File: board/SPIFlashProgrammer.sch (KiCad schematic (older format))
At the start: 0 parts

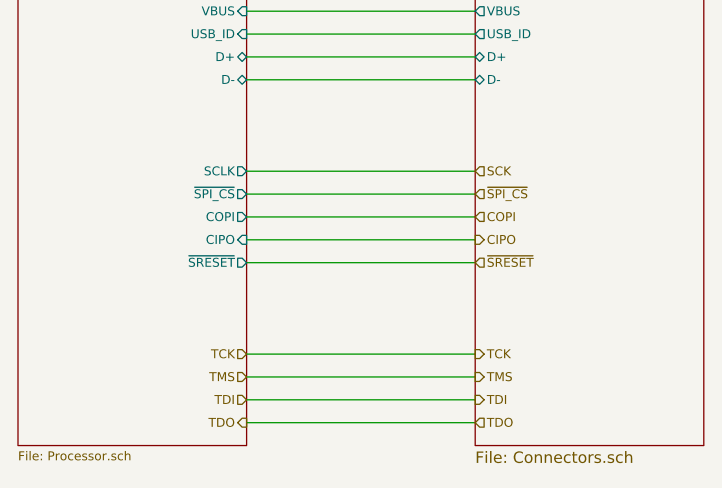
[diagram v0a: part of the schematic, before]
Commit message: Fixed all the top-level wiring that was wrong because the pin types it was connected with were wrong
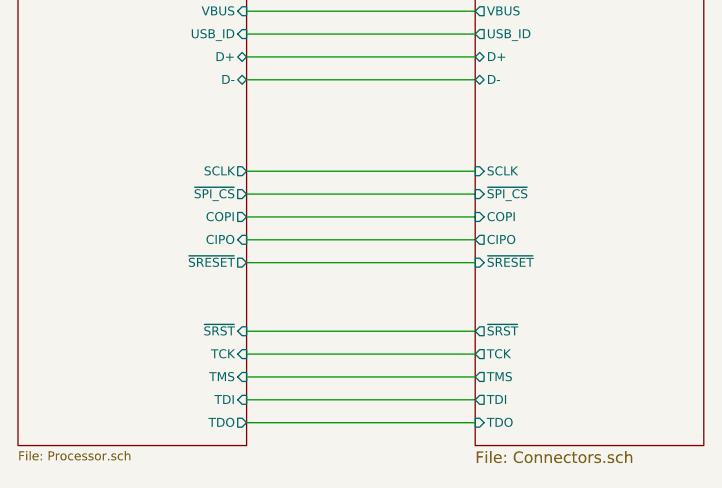
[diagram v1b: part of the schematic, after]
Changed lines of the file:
@@
 Comment4 ""
 $EndDescr
-Text HLabel 5250 5150 0    39   Output ~ 0
-TDO
-Text HLabel 5250 5050 0    39   Input ~ 0
-TDI
-Text HLabel 5250 4950 0    39   Input ~ 0
-TMS
-Text HLabel 5250 4850 0    39   Input ~ 0
-TCK
-Text HLabel 6250 4050 2    39   Input ~ 0
-SCK
-Text HLabel 6250 4150 2    39   Input ~ 0
-~SPI_CS
-Text HLabel 6250 4250 2    39   Input ~ 0
-COPI
-Text HLabel 6250 4350 2    39   Output ~ 0
-CIPO
-Text HLabel 6250 4450 2    39   Input ~ 0
-~SRESET
-Text HLabel 6250 4850 2    39   Output ~ 0
-TCK
-Text HLabel 6250 4950 2    39   Output ~ 0
-TMS
-Text HLabel 6250 5050 2    39   Output ~ 0
-TDI
-Text HLabel 6250 5150 2    39   Input ~ 0
-TDO
 Wire Wire Line
 	5250 3350 6250 3350
@@
 	5250 5150 6250 5150
 $Sheet
+S 6250 3250 1000 2000
+U 5F0A82B6
+F0 "Connectors" 50
+F1 "Connectors.sch" 50
+F2 "D-" B L 6250 3650 39
+F3 "D+" B L 6250 3550 39
+F4 "USB_ID" O L 6250 3450 39
+F5 "VBUS" O L 6250 3350 39
+F6 "CIPO" O L 6250 4350 39
+F7 "SCLK" I L 6250 4050 39
+F8 "~SPI_CS" I L 6250 4150 39
+F9 "~SRESET" I L 6250 4450 39
+F10 "COPI" I L 6250 4250 39
+F11 "TMS" O L 6250 4950 39
+F12 "TCK" O L 6250 4850 39
+F13 "TDO" I L 6250 5150 39
+F14 "TDI" O L 6250 5050 39
+F15 "~SRST" O L 6250 4750 39
+$EndSheet
+$Sheet
 S 4250 3250 1000 2000
 U 5F0A81B1
@@
 F9 "D-" B R 5250 3650 39
 F10 "D+" B R 5250 3550 39
+F11 "TCK" I R 5250 4850 39
+F12 "TMS" I R 5250 4950 39
+F13 "TDI" I R 5250 5050 39
+F14 "TDO" O R 5250 5150 39
+F15 "~SRST" I R 5250 4750 39
 $EndSheet
-$Sheet
-S 6250 3250 1000 2000
-U 5F0A82B6
-F0 "Connectors" 50
-F1 "Connectors.sch" 50
-F2 "D-" B L 6250 3650 39
-F3 "D+" B L 6250 3550 39
-F4 "USB_ID" O L 6250 3450 39
-F5 "VBUS" O L 6250 3350 39
-$EndSheet
+Wire Wire Line
+	5250 4750 6250 4750
 $EndSCHEMATC

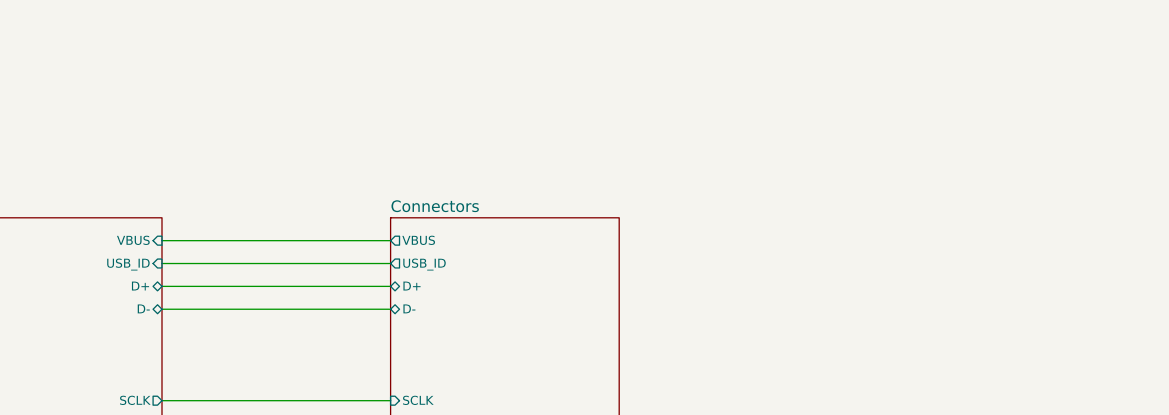
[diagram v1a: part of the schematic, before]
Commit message: Added the work to the schematic from the last stream, and updated all the footprints to reflect the work going in on my symbol and footprint libraries
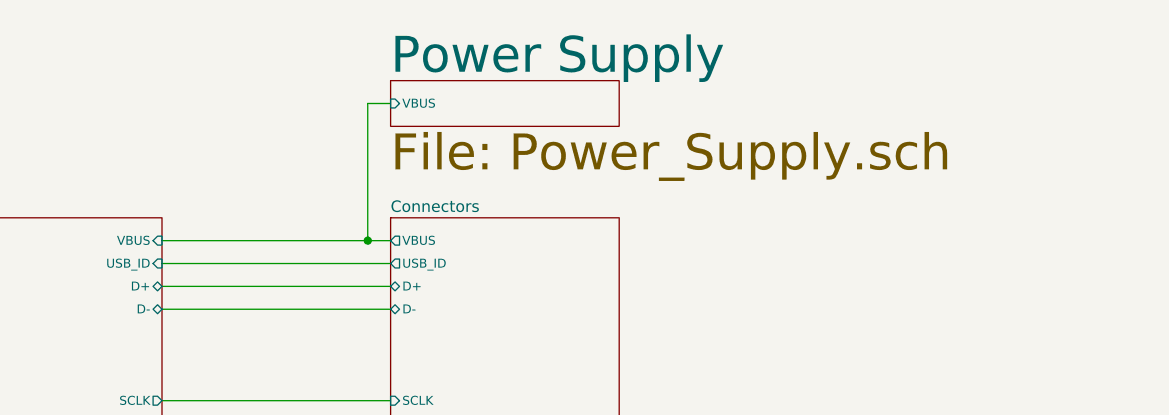
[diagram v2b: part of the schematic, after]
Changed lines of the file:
@@
 $Descr A4 11693 8268
 encoding utf-8
-Sheet 1 3
-Title ""
+Sheet 1 4
+Title "Top-level Schematic"
 Date ""
-Rev ""
-Comp ""
+Rev "R1"
+Comp "Rachel Mant"
 Comment1 ""
 Comment2 ""
@@
 $EndDescr
 Wire Wire Line
-	5250 3350 6250 3350
+	5250 3350 6150 3350
 Wire Wire Line
 	6250 3450 5250 3450
@@
 Wire Wire Line
 	5250 4750 6250 4750
+$Sheet
+S 6250 2650 1000 200
+U 5F6E308F
+F0 "Power Supply" 157
+F1 "Power_Supply.sch" 157
+F2 "VBUS" I L 6250 2750 39
+$EndSheet
+Wire Wire Line
+	6250 2750 6150 2750
+Wire Wire Line
+	6150 2750 6150 3350
+Connection ~ 6150 3350
+Wire Wire Line
+	6150 3350 6250 3350
 $EndSCHEMATC

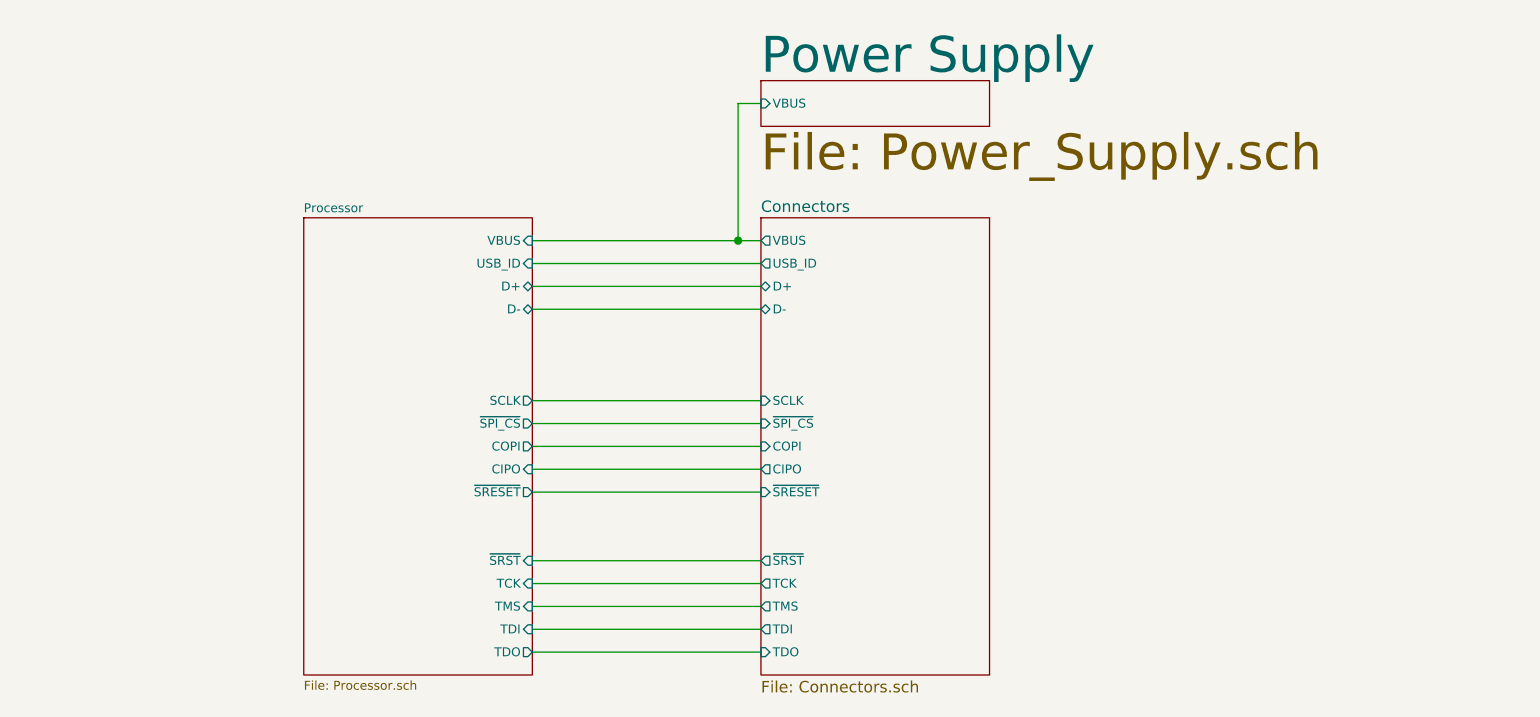
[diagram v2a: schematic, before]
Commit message: Added the two Flash devices and the user buttons to the schematic
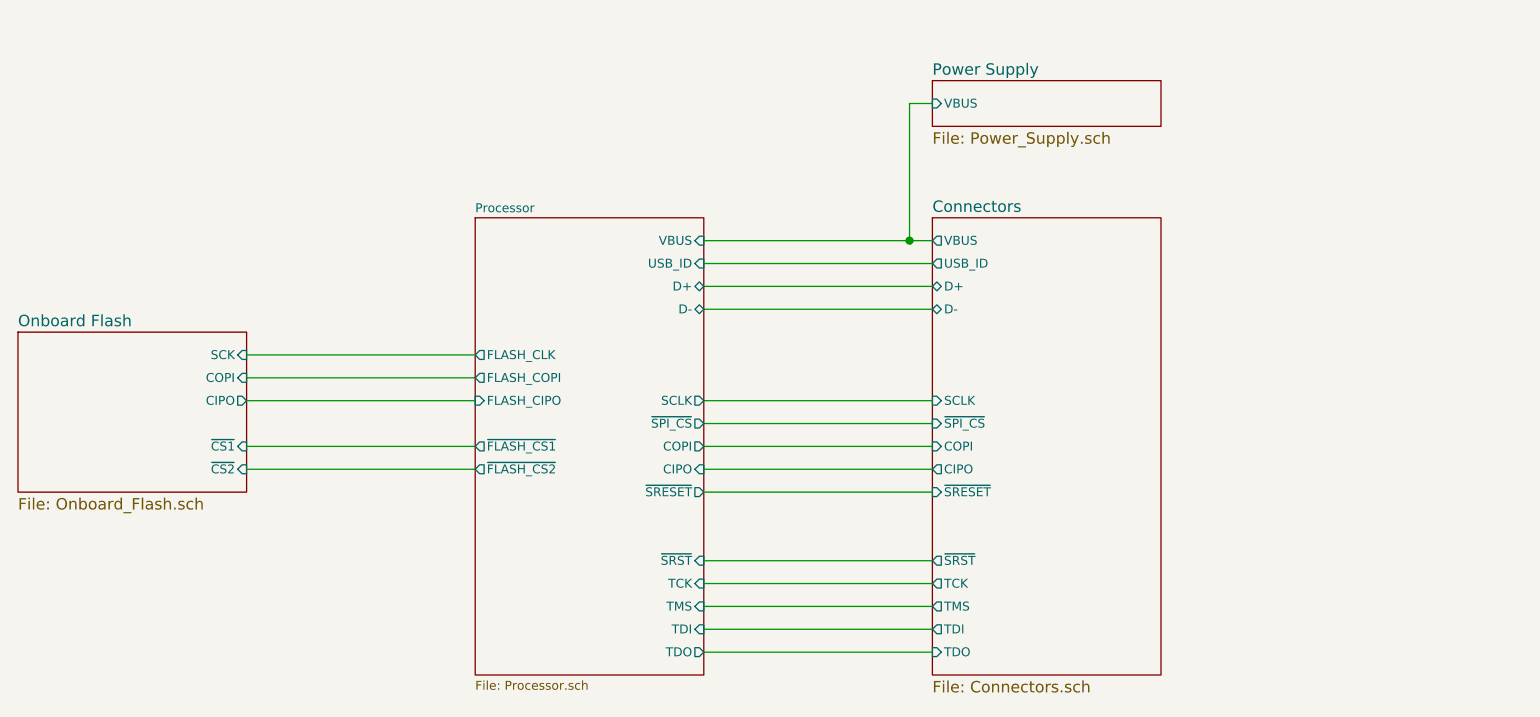
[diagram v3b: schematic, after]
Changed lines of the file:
@@
 $Descr A4 11693 8268
 encoding utf-8
-Sheet 1 4
+Sheet 1 5
 Title "Top-level Schematic"
 Date ""
@@
 $EndDescr
 Wire Wire Line
-	5250 3350 6150 3350
+	6000 3350 6900 3350
 Wire Wire Line
-	6250 3450 5250 3450
+	7000 3450 6000 3450
 Wire Wire Line
-	5250 3550 6250 3550
+	6000 3550 7000 3550
 Wire Wire Line
-	6250 3650 5250 3650
+	7000 3650 6000 3650
 Wire Wire Line
-	5250 4050 6250 4050
+	6000 4050 7000 4050
 Wire Wire Line
-	6250 4150 5250 4150
+	7000 4150 6000 4150
 Wire Wire Line
-	5250 4250 6250 4250
+	6000 4250 7000 4250
 Wire Wire Line
-	6250 4350 5250 4350
+	7000 4350 6000 4350
 Wire Wire Line
-	5250 4450 6250 4450
+	6000 4450 7000 4450
 Wire Wire Line
-	6250 4850 5250 4850
+	7000 4850 6000 4850
 Wire Wire Line
-	5250 4950 6250 4950
+	6000 4950 7000 4950
 Wire Wire Line
-	6250 5050 5250 5050
+	7000 5050 6000 5050
 Wire Wire Line
-	5250 5150 6250 5150
+	6000 5150 7000 5150
 $Sheet
-S 6250 3250 1000 2000
+S 7000 3250 1000 2000
 U 5F0A82B6
 F0 "Connectors" 50
 F1 "Connectors.sch" 50
-F2 "D-" B L 6250 3650 39
-F3 "D+" B L 6250 3550 39
-F4 "USB_ID" O L 6250 3450 39
-F5 "VBUS" O L 6250 3350 39
-F6 "CIPO" O L 6250 4350 39
-F7 "SCLK" I L 6250 4050 39
-F8 "~SPI_CS" I L 6250 4150 39
-F9 "~SRESET" I L 6250 4450 39
-F10 "COPI" I L 6250 4250 39
-F11 "TMS" O L 6250 4950 39
-F12 "TCK" O L 6250 4850 39
-F13 "TDO" I L 6250 5150 39
-F14 "TDI" O L 6250 5050 39
-F15 "~SRST" O L 6250 4750 39
+F2 "D-" B L 7000 3650 39
+F3 "D+" B L 7000 3550 39
+F4 "USB_ID" O L 7000 3450 39
+F5 "VBUS" O L 7000 3350 39
+F6 "CIPO" O L 7000 4350 39
+F7 "SCLK" I L 7000 4050 39
+F8 "~SPI_CS" I L 7000 4150 39
+F9 "~SRESET" I L 7000 4450 39
+F10 "COPI" I L 7000 4250 39
+F11 "TMS" O L 7000 4950 39
+F12 "TCK" O L 7000 4850 39
+F13 "TDO" I L 7000 5150 39
+F14 "TDI" O L 7000 5050 39
+F15 "~SRST" O L 7000 4750 39
 $EndSheet
 $Sheet
-S 4250 3250 1000 2000
+S 5000 3250 1000 2000
 U 5F0A81B1
 F0 "Processor" 39
 F1 "Processor.sch" 39
-F2 "SCLK" O R 5250 4050 39
-F3 "~SPI_CS" O R 5250 4150 39
-F4 "COPI" O R 5250 4250 39
-F5 "CIPO" I R 5250 4350 39
-F6 "~SRESET" O R 5250 4450 39
-F7 "USB_ID" I R 5250 3450 39
-F8 "VBUS" I R 5250 3350 39
-F9 "D-" B R 5250 3650 39
-F10 "D+" B R 5250 3550 39
-F11 "TCK" I R 5250 4850 39
-F12 "TMS" I R 5250 4950 39
-F13 "TDI" I R 5250 5050 39
-F14 "TDO" O R 5250 5150 39
-F15 "~SRST" I R 5250 4750 39
+F2 "SCLK" O R 6000 4050 39
+F3 "~SPI_CS" O R 6000 4150 39
+F4 "COPI" O R 6000 4250 39
+F5 "CIPO" I R 6000 4350 39
+F6 "~SRESET" O R 6000 4450 39
+F7 "USB_ID" I R 6000 3450 39
+F8 "VBUS" I R 6000 3350 39
+F9 "D-" B R 6000 3650 39
+F10 "D+" B R 6000 3550 39
+F11 "TCK" I R 6000 4850 39
+F12 "TMS" I R 6000 4950 39
+F13 "TDI" I R 6000 5050 39
+F14 "TDO" O R 6000 5150 39
+F15 "~SRST" I R 6000 4750 39
+F16 "FLASH_CIPO" I L 5000 4050 39
+F17 "FLASH_COPI" O L 5000 3950 39
+F18 "FLASH_CLK" O L 5000 3850 39
+F19 "~FLASH_CS1" O L 5000 4250 39
+F20 "~FLASH_CS2" O L 5000 4350 39
 $EndSheet
 Wire Wire Line
-	5250 4750 6250 4750
+	6000 4750 7000 4750
 $Sheet
-S 6250 2650 1000 200
+S 7000 2650 1000 200
 U 5F6E308F
-F0 "Power Supply" 157
-F1 "Power_Supply.sch" 157
-F2 "VBUS" I L 6250 2750 39
+F0 "Power Supply" 50
+F1 "Power_Supply.sch" 50
+F2 "VBUS" I L 7000 2750 39
 $EndSheet
 Wire Wire Line
-	6250 2750 6150 2750
+	7000 2750 6900 2750
 Wire Wire Line
-	6150 2750 6150 3350
-Connection ~ 6150 3350
+	6900 2750 6900 3350
+Connection ~ 6900 3350
 Wire Wire Line
-	6150 3350 6250 3350
+	6900 3350 7000 3350
+$Sheet
+S 3000 3750 1000 700
+U 5F8B7B2C
+F0 "Onboard Flash" 50
+F1 "Onboard_Flash.sch" 50
+F2 "SCK" I R 4000 3850 39
+F3 "COPI" I R 4000 3950 39
+F4 "CIPO" O R 4000 4050 39
+F5 "~CS1" I R 4000 4250 39
+F6 "~CS2" I R 4000 4350 39
+$EndSheet
+Wire Wire Line
+	4000 3850 5000 3850
+Wire Wire Line
+	5000 3950 4000 3950
+Wire Wire Line
+	4000 4050 5000 4050
+Wire Wire Line
+	5000 4250 4000 4250
+Wire Wire Line
+	4000 4350 5000 4350
 $EndSCHEMATC

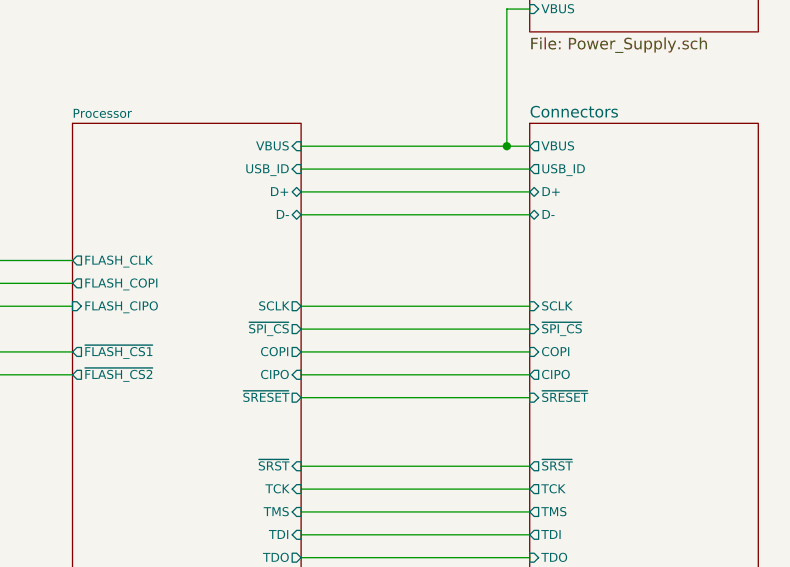
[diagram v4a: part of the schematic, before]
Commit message: Added a SPI present signal for the external bus to the CPU to make detection easier
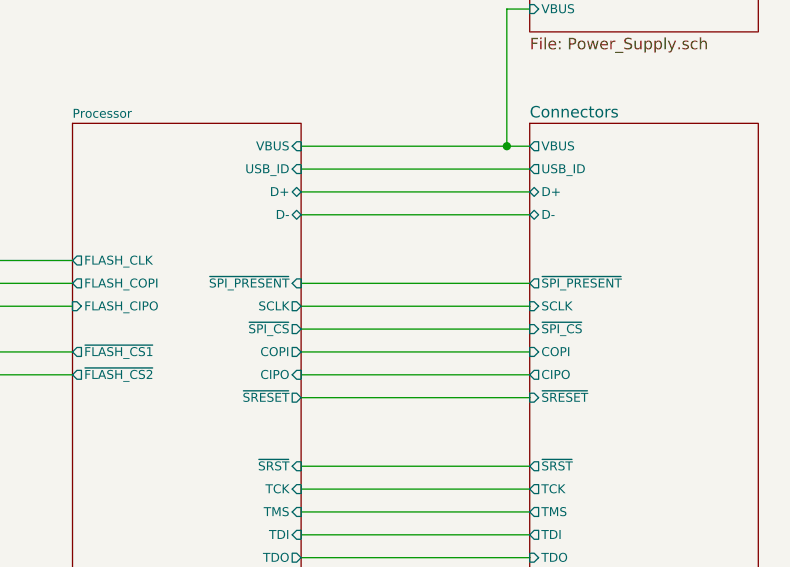
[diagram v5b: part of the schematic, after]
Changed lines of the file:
@@
 F14 "TDI" O L 7000 5050 39
 F15 "~SRST" O L 7000 4750 39
+F16 "~SPI_PRESENT" O L 7000 3950 39
 $EndSheet
 Wire Wire Line
@@
 F19 "~FLASH_CS1" O L 5000 4250 39
 F20 "~FLASH_CS2" O L 5000 4350 39
+F21 "~SPI_PRESENT" I R 6000 3950 39
 $EndSheet
 $Sheet
@@
 F6 "~CS2" I R 4000 4350 39
 $EndSheet
+Wire Wire Line
+	6000 3950 7000 3950
 $EndSCHEMATC
